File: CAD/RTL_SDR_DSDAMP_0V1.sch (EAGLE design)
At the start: 45 parts, among them U1 THS4521ID, U2 TPS73601DBVR, U3 BGA416, LNA

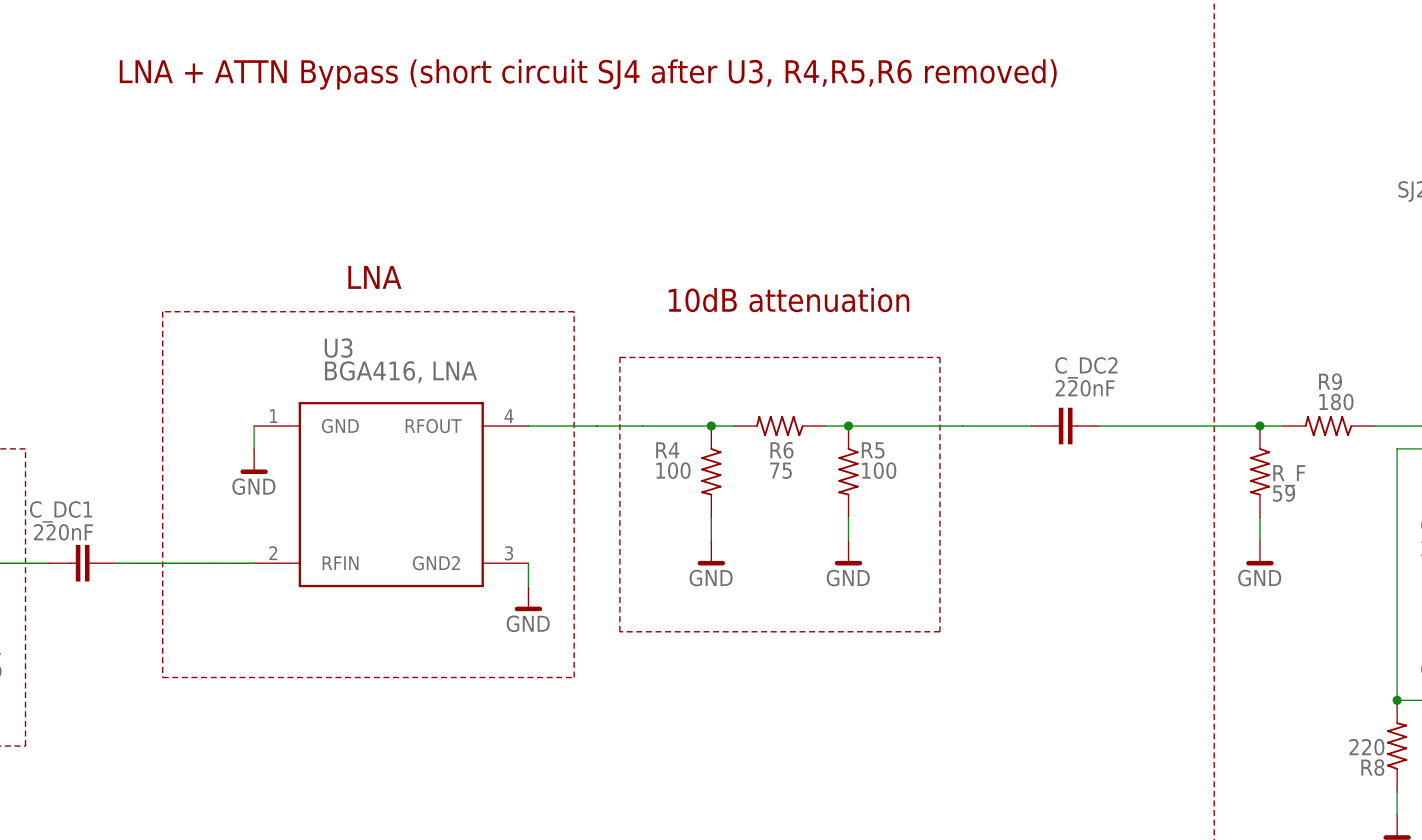
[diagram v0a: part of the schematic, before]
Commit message: Adding the missing LNA VDD bias network, updating CAD / CAM / PDF files
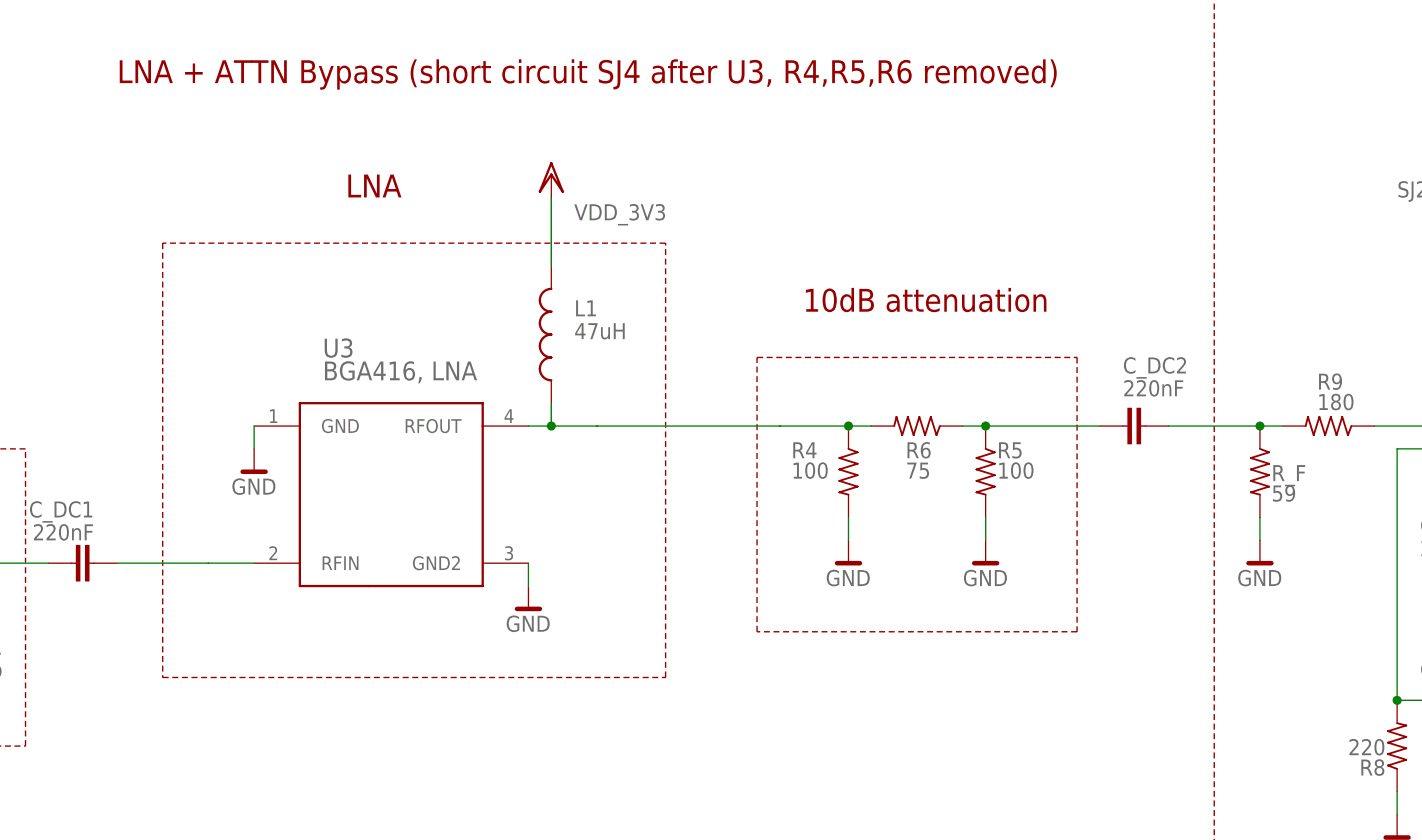
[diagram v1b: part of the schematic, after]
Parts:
- added L1: 47uH, dzo:INDUCTOR_L_1210
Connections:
- net N$2: now also L1.2
- net VDD_3V3: now also L1.1
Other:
- moved on the sheet: C_DC2, R4, R5, R6
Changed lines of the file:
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@@
 <part name="B-" library="dzo" deviceset="TESTPOINT" device="39MIL"/>
 <part name="U$16" library="lve" deviceset="GND" device=""/>
+<part name="L1" library="dzo" deviceset="INDUCTOR_L_1210" device="" value="47uH"/>
+<part name="U$17" library="lve_modositott" deviceset="VDD_3V3" device=""/>
 </parts>
 <sheets>
@@
 <plain>
 <text x="63.5" y="30.48" size="1.778" layer="94">R21 and R22 setup the output voltage.</text>
-<text x="190.5" y="203.2" size="2.54" layer="94">10dB attenuation</text>
-<wire x1="185.42" y1="198.12" x2="220.98" y2="198.12" width="0.1524" layer="94" style="shortdash"/>
-<wire x1="220.98" y1="198.12" x2="220.98" y2="167.64" width="0.1524" layer="94" style="shortdash"/>
-<wire x1="220.98" y1="167.64" x2="185.42" y2="167.64" width="0.1524" layer="94" style="shortdash"/>
-<wire x1="185.42" y1="167.64" x2="185.42" y2="198.12" width="0.1524" layer="94" style="shortdash"/>
+<text x="205.74" y="203.2" size="2.54" layer="94">10dB attenuation</text>
+<wire x1="200.66" y1="198.12" x2="236.22" y2="198.12" width="0.1524" layer="94" style="shortdash"/>
+<wire x1="236.22" y1="198.12" x2="236.22" y2="167.64" width="0.1524" layer="94" style="shortdash"/>
+<wire x1="236.22" y1="167.64" x2="200.66" y2="167.64" width="0.1524" layer="94" style="shortdash"/>
+<wire x1="200.66" y1="167.64" x2="200.66" y2="198.12" width="0.1524" layer="94" style="shortdash"/>
 <wire x1="251.46" y1="246.38" x2="365.76" y2="246.38" width="0.1524" layer="94" style="shortdash"/>
 <wire x1="365.76" y1="246.38" x2="365.76" y2="139.7" width="0.1524" layer="94" style="shortdash"/>
@@
 <wire x1="251.46" y1="139.7" x2="251.46" y2="246.38" width="0.1524" layer="94" style="shortdash"/>
 <text x="289.56" y="248.92" size="2.54" layer="94">Differential Amplifier</text>
-<wire x1="134.62" y1="162.56" x2="180.34" y2="162.56" width="0.1524" layer="94" style="shortdash"/>
-<wire x1="180.34" y1="162.56" x2="180.34" y2="203.2" width="0.1524" layer="94" style="shortdash"/>
-<wire x1="180.34" y1="203.2" x2="134.62" y2="203.2" width="0.1524" layer="94" style="shortdash"/>
-<wire x1="134.62" y1="203.2" x2="134.62" y2="162.56" width="0.1524" layer="94" style="shortdash"/>
-<text x="154.94" y="205.74" size="2.54" layer="94">LNA</text>
+<wire x1="134.62" y1="162.56" x2="190.5" y2="162.56" width="0.1524" layer="94" style="shortdash"/>
+<wire x1="190.5" y1="162.56" x2="190.5" y2="210.82" width="0.1524" layer="94" style="shortdash"/>
+<wire x1="190.5" y1="210.82" x2="134.62" y2="210.82" width="0.1524" layer="94" style="shortdash"/>
+<wire x1="134.62" y1="210.82" x2="134.62" y2="162.56" width="0.1524" layer="94" style="shortdash"/>
+<text x="154.94" y="215.9" size="2.54" layer="94">LNA</text>
 <text x="129.54" y="228.6" size="2.54" layer="94">LNA + ATTN Bypass (short circuit SJ4 after U3, R4,R5,R6 removed)</text>
 <wire x1="58.42" y1="187.96" x2="58.42" y2="154.94" width="0.1524" layer="94" style="shortdash"/>
@@
 <attribute name="NAME" x="20.32" y="185.42" size="1.778" layer="95" rot="R180"/>
 </instance>
-<instance part="R4" gate="G$1" x="195.58" y="185.42" smashed="yes" rot="R270">
-<attribute name="NAME" x="189.23" y="186.9186" size="1.778" layer="95"/>
-<attribute name="VALUE" x="189.23" y="184.658" size="1.778" layer="96"/>
-</instance>
-<instance part="R5" gate="G$1" x="210.82" y="185.42" smashed="yes" rot="R270">
-<attribute name="NAME" x="212.09" y="186.9186" size="1.778" layer="95"/>
-<attribute name="VALUE" x="212.09" y="184.658" size="1.778" layer="96"/>
-</instance>
-<instance part="R6" gate="G$1" x="203.2" y="190.5" smashed="yes" rot="R180">
-<attribute name="NAME" x="201.93" y="186.9186" size="1.778" layer="95"/>
-<attribute name="VALUE" x="201.93" y="184.658" size="1.778" layer="96"/>
-</instance>
-<instance part="U$2" gate="G$1" x="195.58" y="175.26"/>
-<instance part="U$3" gate="G$1" x="210.82" y="175.26"/>
+<instance part="R4" gate="G$1" x="210.82" y="185.42" smashed="yes" rot="R270">
+<attribute name="NAME" x="204.47" y="186.9186" size="1.778" layer="95"/>
+<attribute name="VALUE" x="204.47" y="184.658" size="1.778" layer="96"/>
+</instance>
+<instance part="R5" gate="G$1" x="226.06" y="185.42" smashed="yes" rot="R270">
+<attribute name="NAME" x="227.33" y="186.9186" size="1.778" layer="95"/>
+<attribute name="VALUE" x="227.33" y="184.658" size="1.778" layer="96"/>
+</instance>
+<instance part="R6" gate="G$1" x="218.44" y="190.5" smashed="yes" rot="R180">
+<attribute name="NAME" x="217.17" y="186.9186" size="1.778" layer="95"/>
+<attribute name="VALUE" x="217.17" y="184.658" size="1.778" layer="96"/>
+</instance>
+<instance part="U$2" gate="G$1" x="210.82" y="175.26"/>
+<instance part="U$3" gate="G$1" x="226.06" y="175.26"/>
 <instance part="U3" gate="G$1" x="160.02" y="182.88" smashed="yes">
 <attribute name="NAME" x="152.4" y="198.12" size="2.0828" layer="95" ratio="6" rot="SR0"/>
@@
 <attribute name="VALUE" x="127" y="177.8" size="1.778" layer="96" rot="MR0"/>
 </instance>
-<instance part="C_DC2" gate="G$1" x="233.68" y="190.5" smashed="yes" rot="MR180">
-<attribute name="NAME" x="233.68" y="198.12" size="1.778" layer="95" rot="MR180"/>
-<attribute name="VALUE" x="233.68" y="195.58" size="1.778" layer="96" rot="MR180"/>
+<instance part="C_DC2" gate="G$1" x="241.3" y="190.5" smashed="yes" rot="MR180">
+<attribute name="NAME" x="241.3" y="198.12" size="1.778" layer="95" rot="MR180"/>
+<attribute name="VALUE" x="241.3" y="195.58" size="1.778" layer="96" rot="MR180"/>
 </instance>
 <instance part="C20" gate="G$1" x="276.86" y="172.72" smashed="yes" rot="MR90">
@@
 <instance part="B-" gate="G$1" x="22.86" y="96.52" rot="R180"/>
 <instance part="U$16" gate="G$1" x="25.4" y="91.44"/>
+<instance part="L1" gate="G$1" x="177.8" y="200.66" smashed="yes" rot="MR0">
+<attribute name="NAME" x="180.34" y="204.47" size="1.778" layer="95" rot="MR180"/>
+<attribute name="VALUE" x="180.34" y="201.93" size="1.778" layer="96" rot="MR180"/>
+</instance>
+<instance part="U$17" gate="G$1" x="177.8" y="215.9" smashed="yes">
+<attribute name="VALUE" x="180.34" y="213.36" size="1.778" layer="96"/>
+</instance>
 </instances>
 <busses>
@@
 <pinref part="R4" gate="G$1" pin="2"/>
 <pinref part="U$2" gate="G$1" pin="GND"/>
-<wire x1="195.58" y1="177.8" x2="195.58" y2="180.34" width="0.1524" layer="91"/>
+<wire x1="210.82" y1="177.8" x2="210.82" y2="180.34" width="0.1524" layer="91"/>
 </segment>
 <segment>
 <pinref part="R5" gate="G$1" pin="2"/>
 <pinref part="U$3" gate="G$1" pin="GND"/>
-<wire x1="210.82" y1="177.8" x2="210.82" y2="180.34" width="0.1524" layer="91"/>
+<wire x1="226.06" y1="177.8" x2="226.06" y2="180.34" width="0.1524" layer="91"/>
 </segment>
 <segment>
@@
 <junction x="284.48" y="231.14"/>
 </segment>
+<segment>
+<pinref part="L1" gate="G$1" pin="1"/>
+<wire x1="177.8" y1="208.28" x2="177.8" y2="215.9" width="0.1524" layer="91"/>
+<pinref part="U$17" gate="G$1" pin="VDD_3V3"/>
+</segment>
 </net>
 <net name="N$1" class="0">
@@
 <pinref part="R4" gate="G$1" pin="1"/>
 <pinref part="R6" gate="G$1" pin="2"/>
-<wire x1="198.12" y1="190.5" x2="195.58" y2="190.5" width="0.1524" layer="91"/>
-<wire x1="195.58" y1="190.5" x2="187.96" y2="190.5" width="0.1524" layer="91"/>
-<junction x="195.58" y="190.5"/>
+<wire x1="213.36" y1="190.5" x2="210.82" y2="190.5" width="0.1524" layer="91"/>
+<wire x1="210.82" y1="190.5" x2="203.2" y2="190.5" width="0.1524" layer="91"/>
+<junction x="210.82" y="190.5"/>
 <pinref part="U3" gate="G$1" pin="RFOUT"/>
-<wire x1="175.26" y1="190.5" x2="182.88" y2="190.5" width="0.1524" layer="91"/>
-<wire x1="182.88" y1="190.5" x2="187.96" y2="190.5" width="0.1524" layer="91"/>
+<wire x1="175.26" y1="190.5" x2="177.8" y2="190.5" width="0.1524" layer="91"/>
+<wire x1="177.8" y1="190.5" x2="182.88" y2="190.5" width="0.1524" layer="91"/>
+<wire x1="182.88" y1="190.5" x2="203.2" y2="190.5" width="0.1524" layer="91"/>
+<pinref part="L1" gate="G$1" pin="2"/>
+<wire x1="177.8" y1="193.04" x2="177.8" y2="190.5" width="0.1524" layer="91"/>
+<junction x="177.8" y="190.5"/>
 </segment>
 </net>
@@
 <pinref part="R9" gate="G$1" pin="2"/>
 <pinref part="C_DC2" gate="G$1" pin="2"/>
-<wire x1="238.76" y1="190.5" x2="256.54" y2="190.5" width="0.1524" layer="91"/>
+<wire x1="246.38" y1="190.5" x2="256.54" y2="190.5" width="0.1524" layer="91"/>
 <pinref part="R_F" gate="G$1" pin="1"/>
 <wire x1="256.54" y1="190.5" x2="259.08" y2="190.5" width="0.1524" layer="91"/>
@@
 <segment>
 <pinref part="C_DC2" gate="G$1" pin="1"/>
-<wire x1="223.52" y1="190.5" x2="231.14" y2="190.5" width="0.1524" layer="91"/>
 <pinref part="R5" gate="G$1" pin="1"/>
-<wire x1="210.82" y1="190.5" x2="223.52" y2="190.5" width="0.1524" layer="91"/>
-<junction x="210.82" y="190.5"/>
+<wire x1="226.06" y1="190.5" x2="238.76" y2="190.5" width="0.1524" layer="91"/>
+<junction x="226.06" y="190.5"/>
 <pinref part="R6" gate="G$1" pin="1"/>
-<wire x1="208.28" y1="190.5" x2="210.82" y2="190.5" width="0.1524" layer="91"/>
-</segment>
-</net>
+<wire x1="223.52" y1="190.5" x2="226.06" y2="190.5" width="0.1524" layer="91"/>
+</segment>
+</net>
